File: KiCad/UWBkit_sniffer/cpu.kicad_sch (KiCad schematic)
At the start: 1 part, among them U1 LBUA5QJ2AB

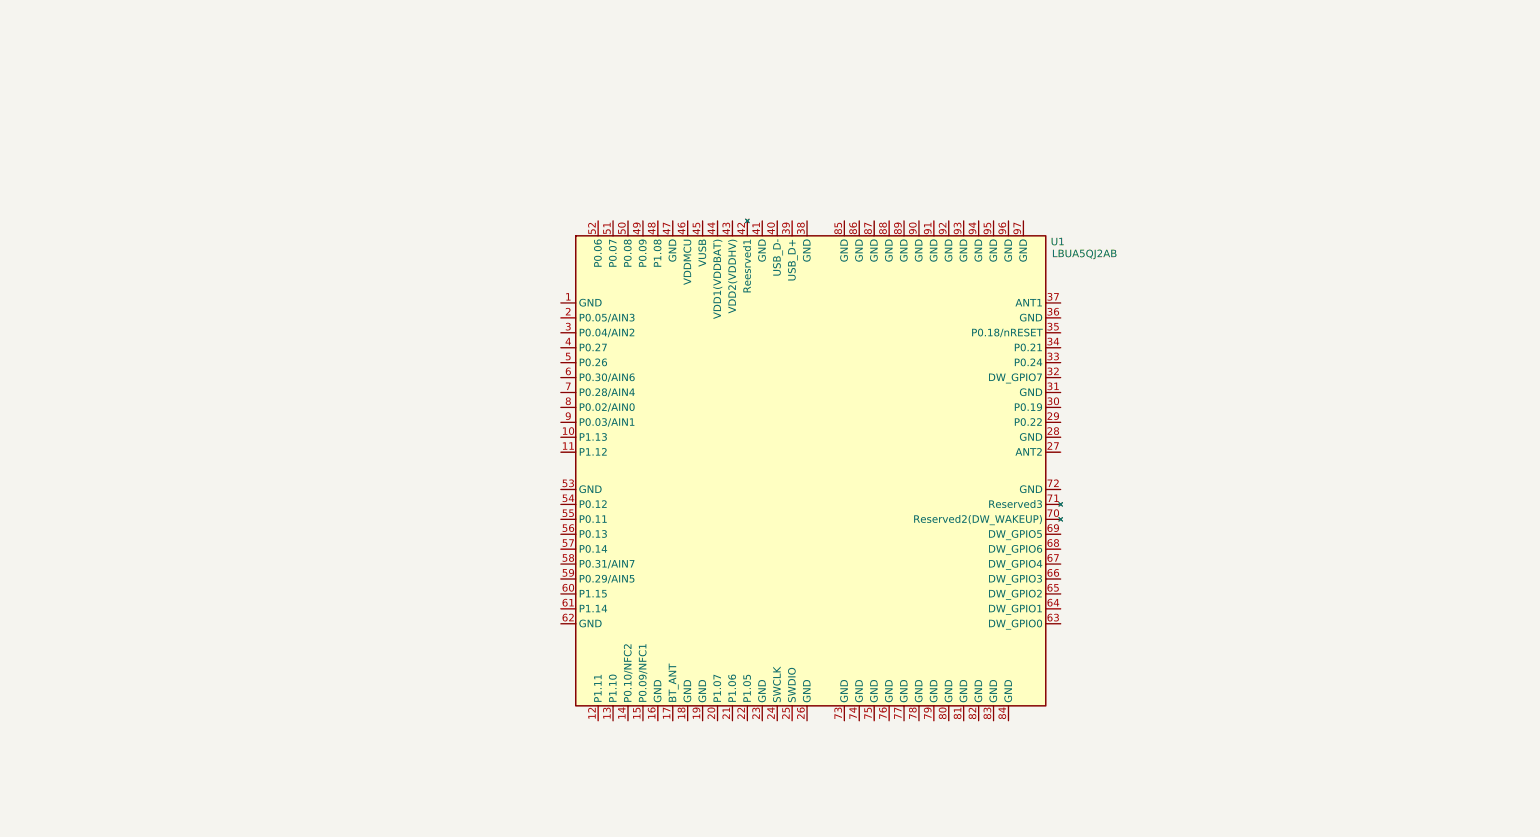
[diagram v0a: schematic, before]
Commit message: Wired connections to SoC
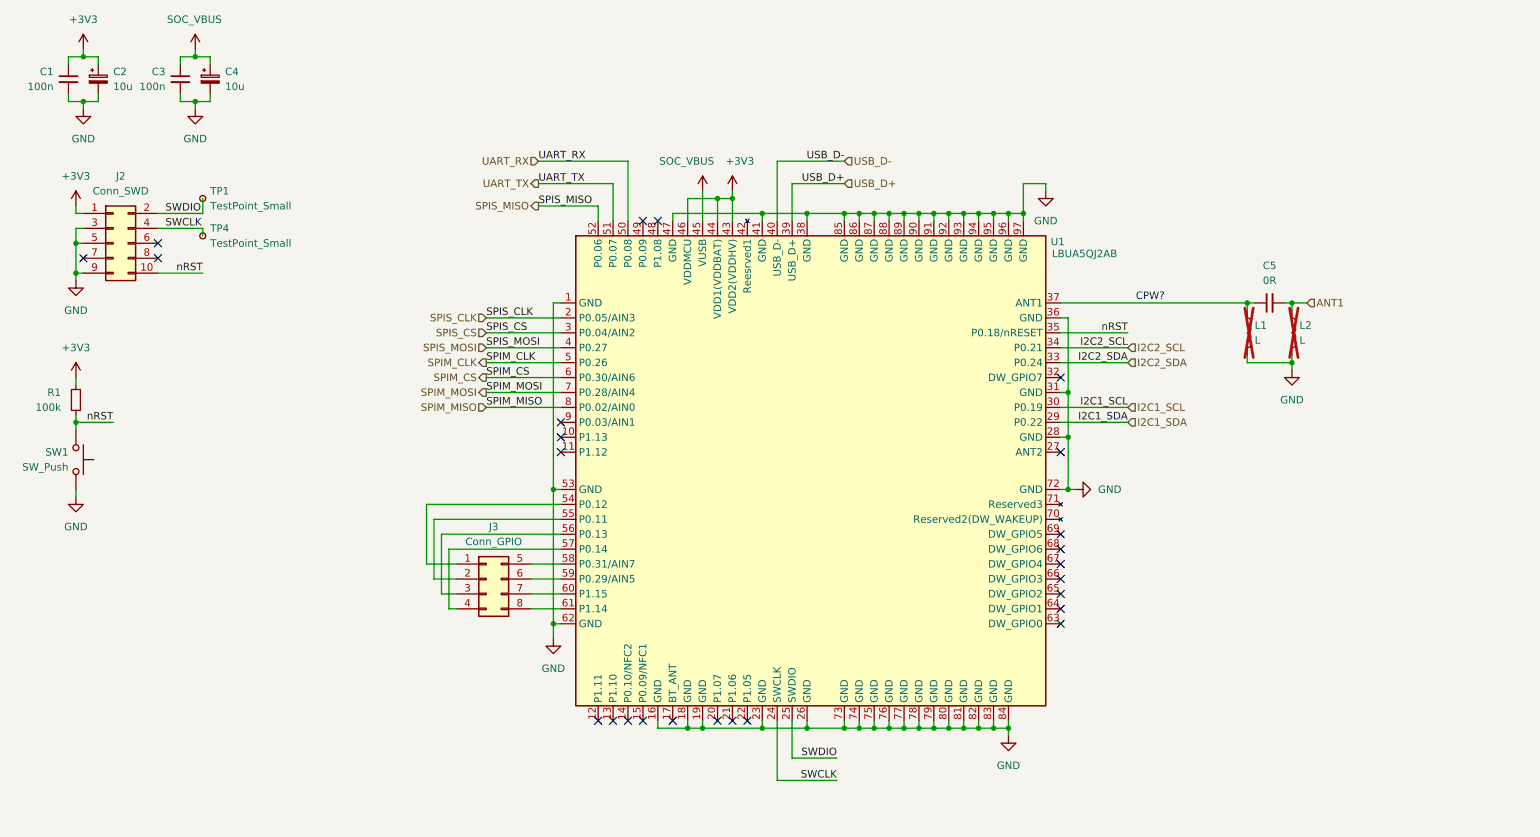
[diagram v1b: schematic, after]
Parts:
- added C1, C3: 100n, Capacitor_SMD:C_0603_1608Metric, symbol Device:C_Small
- added C2, C4: 10u, Capacitor_Tantalum_SMD:CP_EIA-3216-18_Kemet-A, symbol Device:C_Polarized_Small
- added C5: 0R, Capacitor_SMD:C_0603_1608Metric, symbol Device:C_Small
- added J2: Conn_SWD, Connector_PinHeader_1.27mm:PinHeader_2x05_P1.27mm_Vertical_SMD, symbol Connector_Generic:Conn_02x05_Odd_Even
- added J3: Conn_GPIO, Connector_PinSocket_2.54mm:PinSocket_2x04_P2.54mm_Vertical, symbol Connector_Generic:Conn_02x04_Top_Bottom
- added L1, L2: L, Inductor_SMD:L_0603_1608Metric, symbol Device:L
- added R1: 100k, Resistor_SMD:R_0603_1608Metric, symbol Device:R_Small
- added SW1: SW_Push, Button_Switch_THT:SW_TH_Tactile_Omron_B3F-106x, symbol Switch:SW_Push
- added TP1, TP4: TestPoint_Small, TestPoint:TestPoint_Pad_D1.5mm, symbol Connector:TestPoint_Small
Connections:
- net GND: now reaches U1.1 (GND)
- net GND: now also U1.16 (GND), U1.18 (GND), U1.19 (GND), U1.23 (GND), U1.26 (GND), U1.28 (GND), U1.31 (GND), U1.36 (GND), U1.38 (GND), U1.41 (GND), U1.47 (GND), U1.53 (GND), U1.62 (GND), U1.72 (GND), U1.73 (GND), U1.74 (GND), U1.75 (GND), U1.76 (GND), U1.77 (GND), U1.78 (GND), U1.79 (GND), U1.80 (GND), U1.81 (GND), U1.82 (GND), U1.83 (GND), U1.84 (GND), U1.85 (GND), U1.86 (GND), U1.87 (GND), U1.88 (GND), U1.89 (GND), U1.90 (GND), U1.91 (GND), U1.92 (GND), U1.93 (GND), U1.94 (GND), U1.95 (GND), U1.96 (GND), U1.97 (GND), C1.2, C2.2, C3.2, C4.2, J2.3 (Pin_3), J2.5 (Pin_5), J2.9 (Pin_9), L1.2, L2.2, SW1.1
- net SPIS_CLK: now reaches U1.2 (P0.05/AIN3)
- net SWCLK: now reaches U1.24 (SWCLK)
- net SWCLK: now also J2.4 (Pin_4), TP4.1
- net SWDIO: now reaches U1.25 (SWDIO)
- net SWDIO: now also J2.2 (Pin_2), TP1.1
- net I2C1_SDA: now reaches U1.29 (P0.22)
- net SPIS_CS: now reaches U1.3 (P0.04/AIN2)
- net I2C1_SCL: now reaches U1.30 (P0.19)
- net I2C2_SDA: now reaches U1.33 (P0.24)
- net I2C2_SCL: now reaches U1.34 (P0.21)
- net nRST: now reaches U1.35 (P0.18/nRESET)
- net nRST: now also J2.10 (Pin_10), R1.2, SW1.2
- net at U1.37 (ANT1): now also C5.1, L1.1
- net USB_D+: now reaches U1.39 (USB_D+)
- net SPIS_MOSI: now reaches U1.4 (P0.27)
- net USB_D-: now reaches U1.40 (USB_D-)
- net +3V3: now reaches U1.43 (VDD2(VDDHV))
- net +3V3: now also U1.44 (VDD1(VDDBAT)), U1.46 (VDDMCU), C1.1, C2.1, J2.1 (Pin_1), R1.1
- net SOC_VBUS: now reaches U1.45 (VUSB)
- net SOC_VBUS: now also C3.1, C4.1
- net SPIM_CLK: now reaches U1.5 (P0.26)
- net UART_RX: now reaches U1.50 (P0.08)
- net UART_TX: now reaches U1.51 (P0.07)
- net SPIS_MISO: now reaches U1.52 (P0.06)
- net at U1.54 (P0.12): now also J3.1 (Pin_1)
- net at U1.55 (P0.11): now also J3.2 (Pin_2)
- net at U1.56 (P0.13): now also J3.3 (Pin_3)
- net at U1.57 (P0.14): now also J3.4 (Pin_4)
- net at U1.58 (P0.31/AIN7): now also J3.5 (Pin_5)
- net at U1.59 (P0.29/AIN5): now also J3.6 (Pin_6)
- net SPIM_CS: now reaches U1.6 (P0.30/AIN6)
- net at U1.60 (P1.15): now also J3.7 (Pin_7)
- net at U1.61 (P1.14): now also J3.8 (Pin_8)
- net SPIM_MOSI: now reaches U1.7 (P0.28/AIN4)
- net SPIM_MISO: now reaches U1.8 (P0.02/AIN0)
- new net ANT1: C5.2, L2.1
- no-connect marks 0 -> 25
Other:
- note added: "CPW?"

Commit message: Added components to schematic
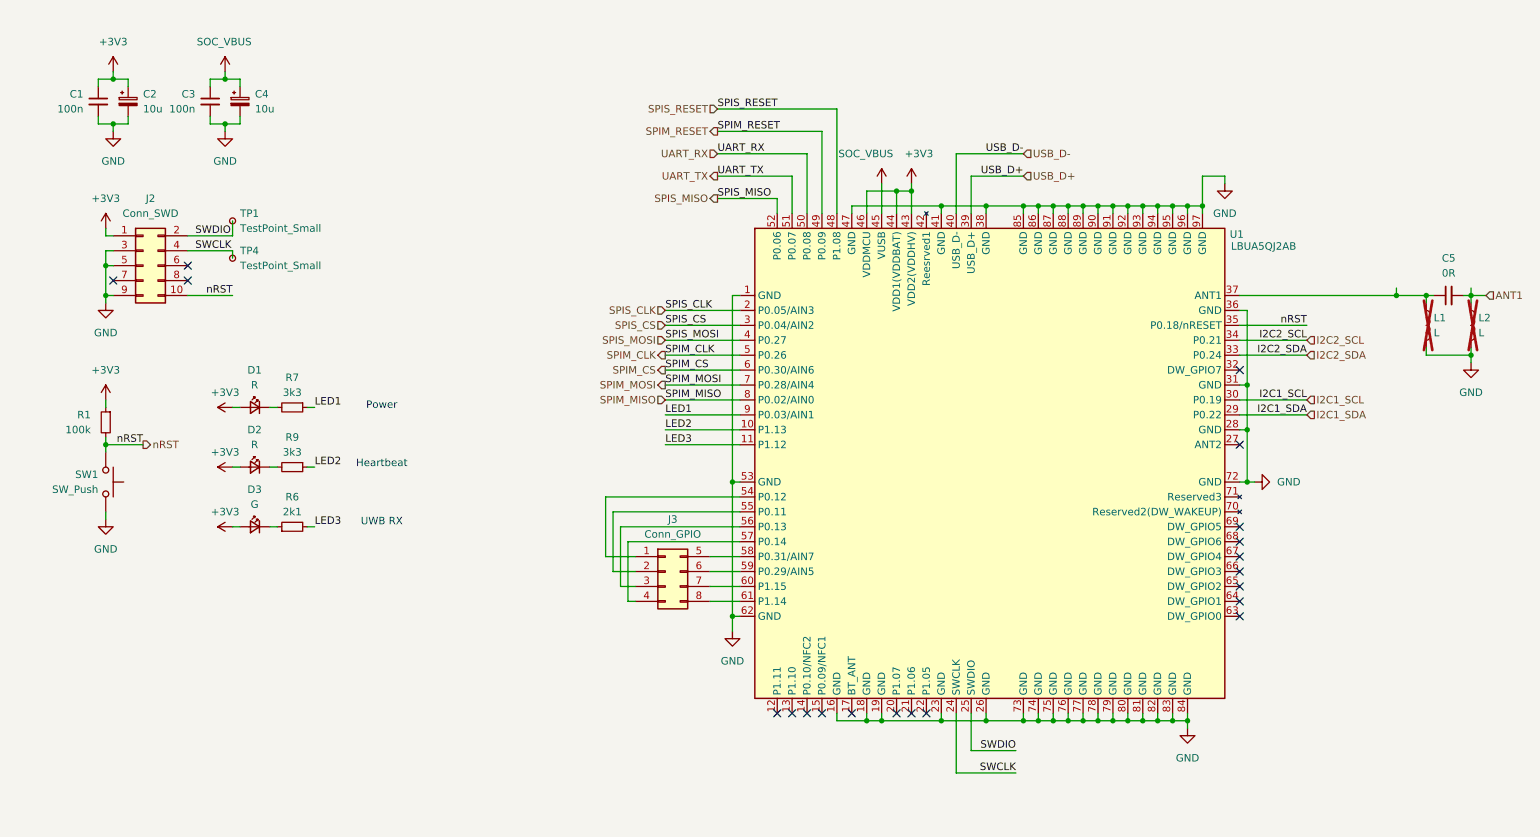
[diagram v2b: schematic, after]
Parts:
- added D1, D2: R, LED_SMD:LED_0603_1608Metric, symbol Device:LED_Small
- added D3: G, LED_SMD:LED_0603_1608Metric, symbol Device:LED_Small
- added R6: 2k1, Resistor_SMD:R_0603_1608Metric, symbol Device:R_Small
- added R7, R9: 3k3, Resistor_SMD:R_0603_1608Metric, symbol Device:R_Small
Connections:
- net +3V3: now also D1.2 (A), D2.2 (A), D3.2 (A)
- net LED2: now reaches U1.10 (P1.13)
- net LED2: now also R9.1
- net LED3: now reaches U1.11 (P1.12)
- net LED3: now also R6.2
- net SPIS_RESET: now reaches U1.48 (P1.08)
- net SPIM_RESET: now reaches U1.49 (P0.09)
- net LED1: now reaches U1.9 (P0.03/AIN1)
- net LED1: now also R7.1
- new net: D1.1 (K), R7.2
- new net: D3.1 (K), R6.1
- new net: D2.1 (K), R9.2
- no-connect marks 25 -> 20
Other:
- note added: "Heartbeat"
- note added: "Power"
- note added: "UWB RX"
- note removed: "CPW?"
- moved on the sheet: C1, C2, C3, C4, C5, J2, J3, L1, L2, R1, SW1, TP1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

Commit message: First version of PCB
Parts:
- added TP2, TP3: TestPoint_Small, TestPoint:TestPoint_Pad_D1.0mm, symbol Connector:TestPoint_Small
- C5: footprint Capacitor_SMD:C_0603_1608Metric -> Capacitor_SMD:C_0402_1005Metric
- L1, L2: footprint Inductor_SMD:L_0603_1608Metric -> Inductor_SMD:L_0402_1005Metric
- TP1, TP4: footprint TestPoint:TestPoint_Pad_D1.5mm -> TestPoint:TestPoint_Pad_D1.0mm
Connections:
- net +3V3: now also TP3.1
- net LED3: now also R6.1; no longer R6.2
- net SOC_VBUS: now also TP2.1
- net at D3.1 (K): now also R6.2; no longer R6.1

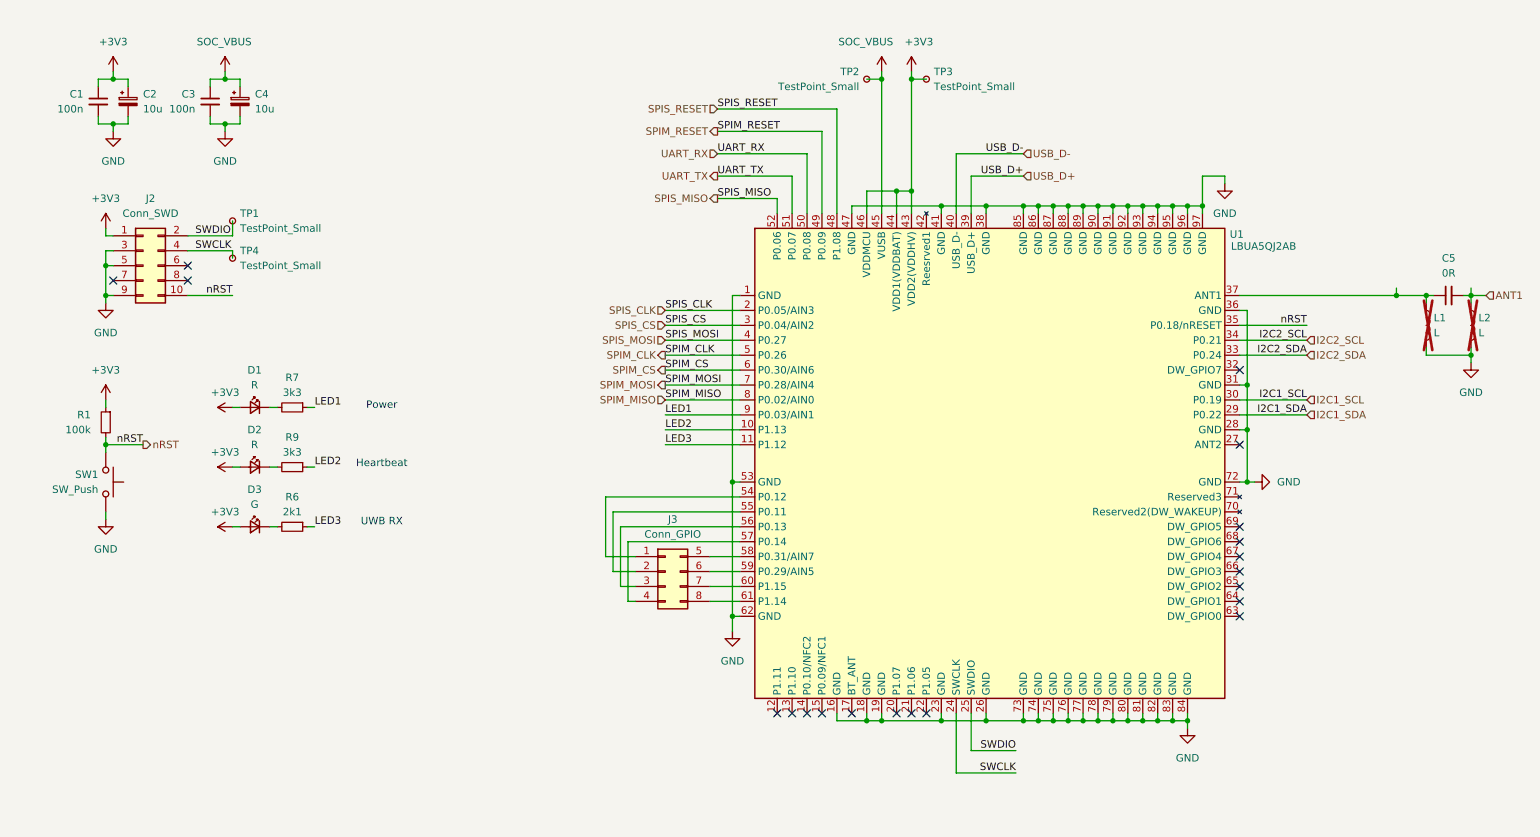
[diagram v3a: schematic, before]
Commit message: United 5V rails, modified layout of connectors
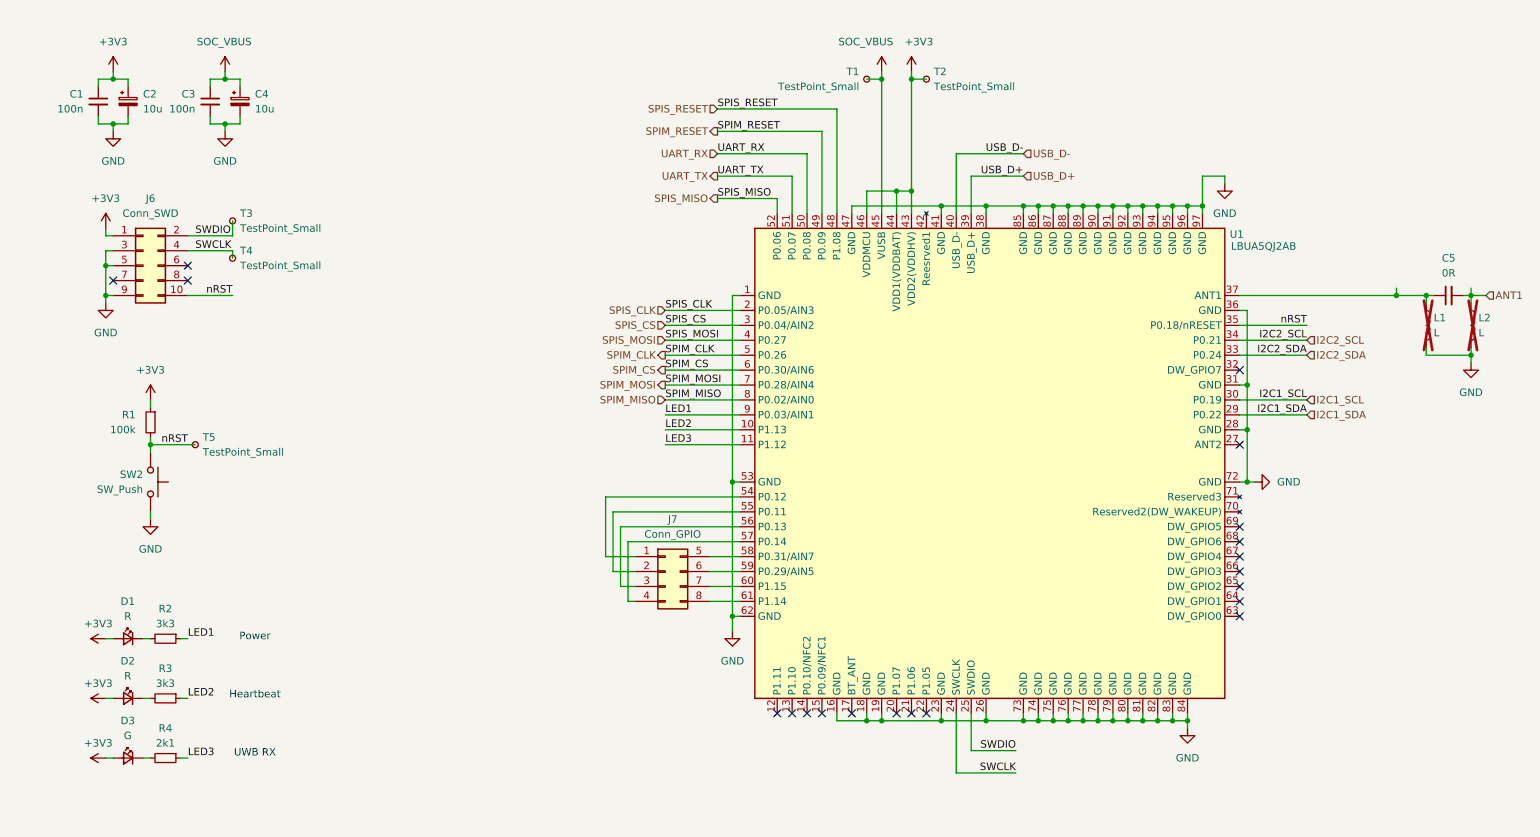
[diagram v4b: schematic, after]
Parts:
- added T5: TestPoint_Small, TestPoint:TestPoint_Pad_D1.0mm, symbol Connector:TestPoint_Small
- renumbered J2 to J6, J3 to J7, R7 to R2, R9 to R3, R6 to R4, SW1 to SW2, TP2 to T1, TP3 to T2, TP1 to T3, TP4 to T4
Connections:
- net nRST: now also T5.1
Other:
- moved on the sheet: D1, D2, D3, R1, R2, R3, R4, SW2

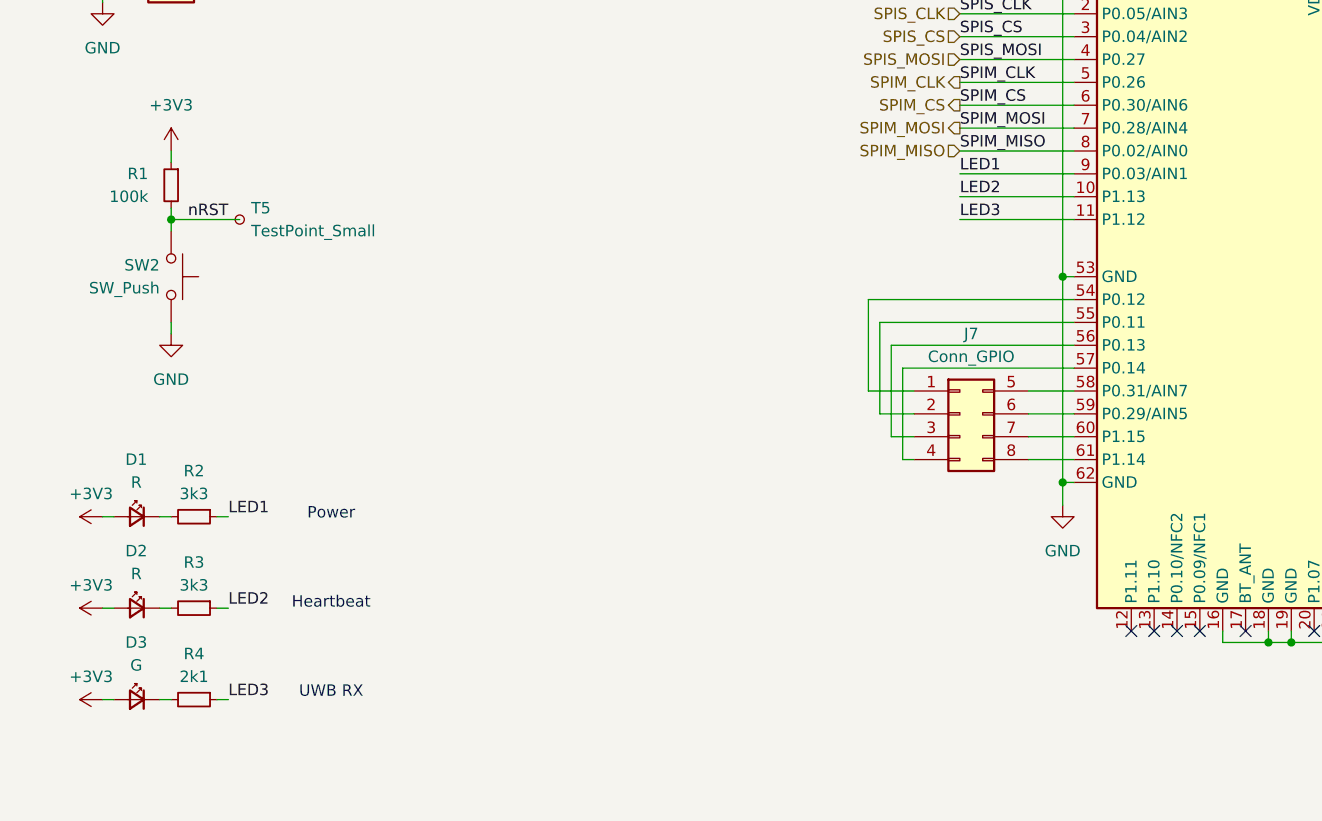
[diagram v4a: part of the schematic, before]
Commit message: Removed UWA.01, added CTS/RTS connections
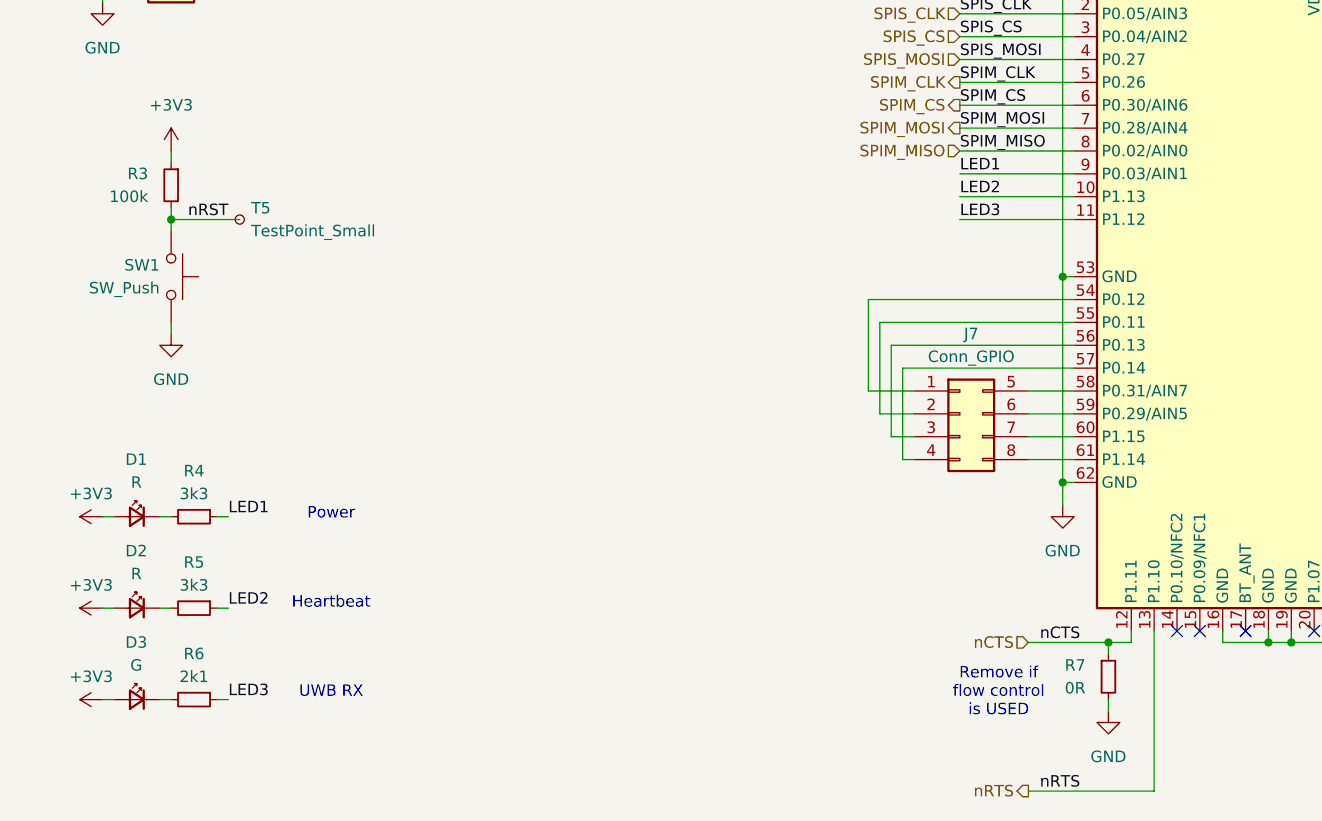
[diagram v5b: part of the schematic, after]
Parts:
- added R7: 0R, Resistor_SMD:R_0603_1608Metric, symbol Device:R_Small
- renumbered R1 to R3, R2 to R4, R3 to R5, R4 to R6, SW2 to SW1
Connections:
- net GND: now also R7.2
- net nCTS: now reaches U1.12 (P1.11)
- net nCTS: now also R7.1
- net nRTS: now reaches U1.13 (P1.10)
- no-connect marks 20 -> 18
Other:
- note added: "Remove if flow control is USED"
